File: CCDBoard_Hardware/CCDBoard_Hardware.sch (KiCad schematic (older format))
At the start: 19 parts

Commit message: Further Edits
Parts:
- removed C? (x3): C_Small, symbol Device:C_Small
- removed C? (x3): CP_Small, symbol Device:CP_Small
- added C? (x2): 0.1 µF, symbol Device:C_Small
- added C? (x2): 22 µF/25 V, symbol Device:CP_Small
- added Conn?: Molex_SL_04 IN, symbol MRDT_Connectors:Molex_SL_04
- added Conn?: Molex_SL_04 OUT, symbol MRDT_Connectors:Molex_SL_04
- added TP?: VideoTestPoint, symbol Connector:TestPoint
- added TP?: TrigTestPoint, symbol Connector:TestPoint
- added TP?: EOSTestPoint, symbol Connector:TestPoint
- added U?: LT1818, symbol pspice:OPAMP
- C? (x2): value C_Small -> 0.1 µF
- C? (x2): value CP_Small -> 22 µF/25 V
- C?: value C_Small -> 1 µF
- C?: value C_Small -> 22 pF
- R? (x2): value R -> 82 Ω
- R?: value R -> 100 Ω
- R?: value R -> 51 Ω
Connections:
- net +5V: now also C?.1, C?.1, C?.1, C?.1, Conn?.1, U?.4 (V+); no longer U?.~ (V-)
- net -IN: no longer R?.1
- net CLK: now also Conn?.3; no longer R?.2
- net EOS: now also Conn?.2, TP?.1; no longer U?.~ (Vss)
- net GND: now also C?.2, C?.2, C?.2, C?.2, Conn?.4, Conn?.4, U?.5 (V-)
- net ST: now also Conn?.2; no longer R?.1
- net Trig: now also Conn?.1, TP?.1; no longer U?.~ (Vss)
- net Video: now also Conn?.3, TP?.1; no longer R?.1
- net Trig_OUT: now reaches U?.~ (Vss)
- net Trig_OUT: now also U?.~ (Vcc)
- new net: R?.1, U?.1 (+)
- new net: R?.1, U?.2 (-), U?.3
- new net CLK_IN: R?.2, U?.~ (Vcc)
- new net EOS_OUT: U?.~ (Vcc), U?.~ (Vss)
- new net ST_IN: R?.1, U?.~ (Vcc)
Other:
- moved on the sheet: C?, R?, U?

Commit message: Added test points
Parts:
- removed U?: LT1818, symbol MRDT_ICs:LT1818
- added TP4: VideoPreAmpTestPoint, symbol Connector:TestPoint
- added TP5: CLKTestPoint, symbol Connector:TestPoint
- added TP6: STTestPoint, symbol Connector:TestPoint
- gave numbers to parts that had none: 22
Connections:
- net CLK: now also TP5.1
- net ST: now also TP6.1
- net at R3.2, U1.~ (Vss): now also TP4.1
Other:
- moved on the sheet: C6, C7, C8, R3, R4, TP1, U2

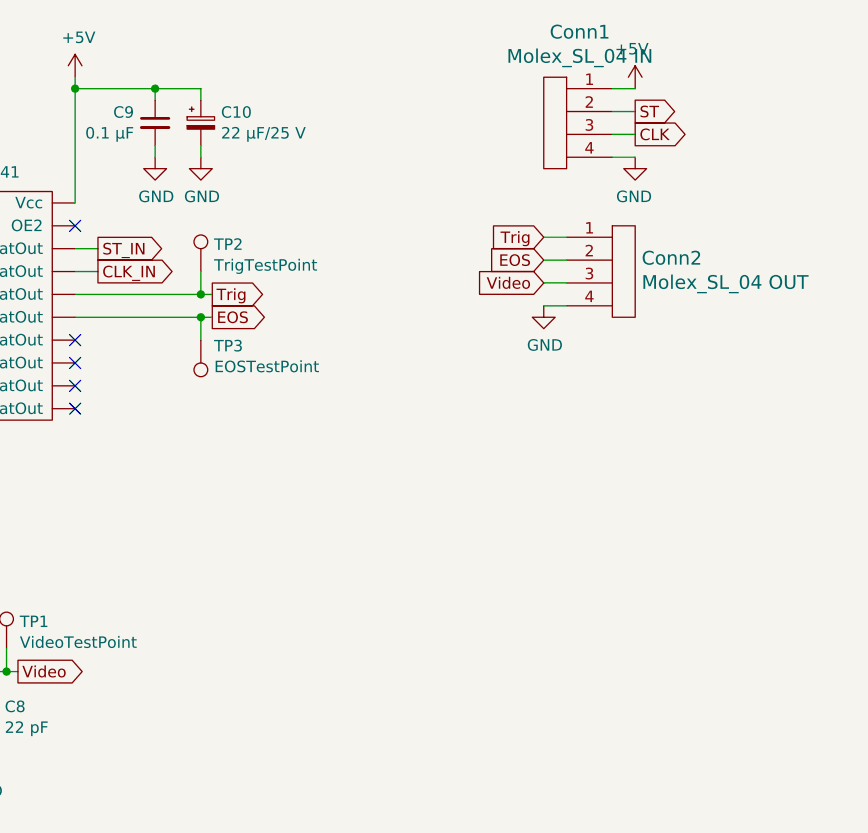
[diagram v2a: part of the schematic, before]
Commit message: Created and assigned footprints
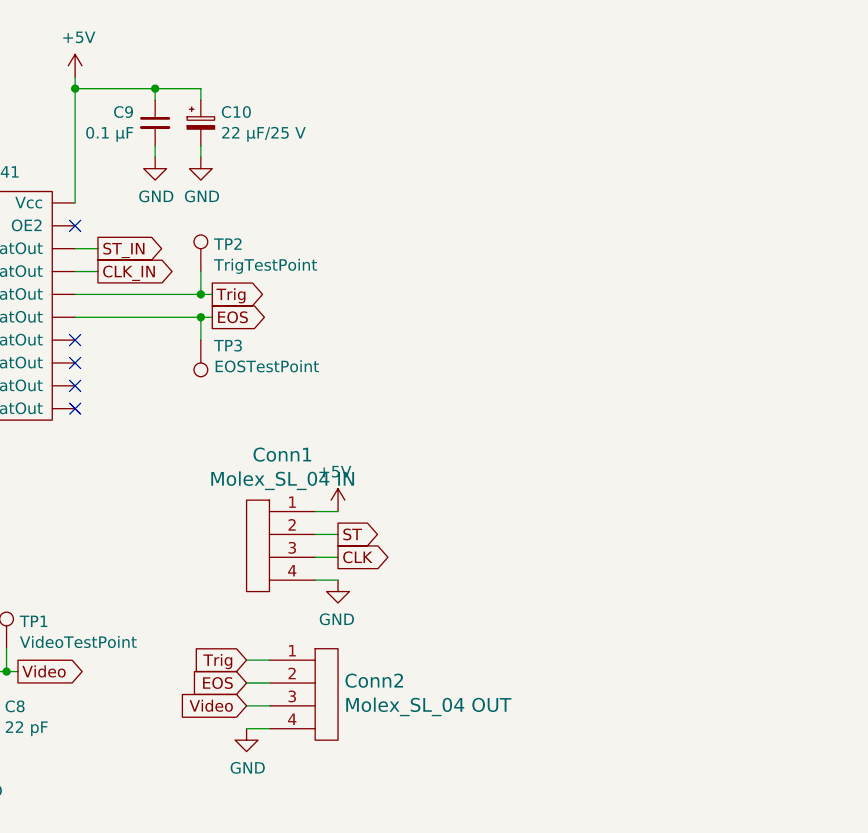
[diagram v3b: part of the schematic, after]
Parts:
- C1, C10, C4, C7: footprint (none) -> Capacitor_SMD:C_0805_2012Metric_Pad1.15x1.40mm_HandSolder
- C2, C3, C5, C6, C8, C9: footprint (none) -> Capacitor_SMD:C_0603_1608Metric_Pad1.05x0.95mm_HandSolder
- Conn1, Conn2: footprint (none) -> MRDT_Connectors:MOLEX_SL_04_Vertical
- R1, R2, R3, R4: footprint (none) -> Resistor_SMD:R_0603_1608Metric_Pad1.05x0.95mm_HandSolder
- TP1, TP2, TP3, TP4, TP5, TP6: footprint (none) -> TestPoint:TestPoint_THTPad_D2.5mm_Drill1.2mm
- U1: footprint (none) -> MRDT_Devices:CCD-S11639-01
- U2: footprint (none) -> Package_TO_SOT_SMD:SOT-23-5_HandSoldering
- U3: footprint (none) -> Package_SO:SOIC-20W_7.5x12.8mm_P1.27mm
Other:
- moved on the sheet: Conn1, Conn2
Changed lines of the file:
@@
 F 0 "U1" H 2950 2525 50  0000 C CNN
 F 1 "S11639-01" H 2950 2434 50  0000 C CNN
-F 2 "" H 2950 2400 50  0001 C CNN
+F 2 "MRDT_Devices:CCD-S11639-01" H 2950 2400 50  0001 C CNN
 F 3 "" H 2950 2400 50  0001 C CNN
 	1    2950 2400
@@
 F 0 "C3" H 2892 1946 50  0000 L CNN
 F 1 "0.1 µF" H 2892 1855 50  0000 L CNN
-F 2 "" H 2800 1900 50  0001 C CNN
+F 2 "Capacitor_SMD:C_0603_1608Metric_Pad1.05x0.95mm_HandSolder" H 2800 1900 50  0001 C CNN
 F 3 "~" H 2800 1900 50  0001 C CNN
 	1    2800 1900
@@
 F 0 "C4" H 3088 1946 50  0000 L CNN
 F 1 "22 µF/25 V" H 3088 1855 50  0000 L CNN
-F 2 "" H 3000 1900 50  0001 C CNN
+F 2 "Capacitor_SMD:C_0805_2012Metric_Pad1.15x1.40mm_HandSolder" H 3000 1900 50  0001 C CNN
 F 3 "~" H 3000 1900 50  0001 C CNN
 	1    3000 1900
@@
 F 0 "R1" V 2515 2700 50  0000 C CNN
 F 1 "82 Ω" V 2606 2700 50  0000 C CNN
-F 2 "" V 2330 2700 50  0001 C CNN
+F 2 "Resistor_SMD:R_0603_1608Metric_Pad1.05x0.95mm_HandSolder" V 2330 2700 50  0001 C CNN
 F 3 "~" H 2400 2700 50  0001 C CNN
 	1    2400 2700
@@
 F 0 "R2" V 3343 2500 50  0000 C CNN
 F 1 "82 Ω" V 3434 2500 50  0000 C CNN
-F 2 "" V 3480 2500 50  0001 C CNN
+F 2 "Resistor_SMD:R_0603_1608Metric_Pad1.05x0.95mm_HandSolder" V 3480 2500 50  0001 C CNN
 F 3 "~" H 3550 2500 50  0001 C CNN
 	1    3550 2500
@@
 F 0 "C5" H 3542 2896 50  0000 L CNN
 F 1 "1 µF" H 3542 2805 50  0000 L CNN
-F 2 "" H 3450 2850 50  0001 C CNN
+F 2 "Capacitor_SMD:C_0603_1608Metric_Pad1.05x0.95mm_HandSolder" H 3450 2850 50  0001 C CNN
 F 3 "~" H 3450 2850 50  0001 C CNN
 	1    3450 2850
@@
 F 0 "C1" H 2088 3896 50  0000 L CNN
 F 1 "22 µF/25 V" H 2088 3805 50  0000 L CNN
-F 2 "" H 2000 3850 50  0001 C CNN
+F 2 "Capacitor_SMD:C_0805_2012Metric_Pad1.15x1.40mm_HandSolder" H 2000 3850 50  0001 C CNN
 F 3 "~" H 2000 3850 50  0001 C CNN
 	1    2000 3850
@@
 F 0 "C2" H 2292 3896 50  0000 L CNN
 F 1 "0.1 µF" H 2292 3805 50  0000 L CNN
-F 2 "" H 2200 3850 50  0001 C CNN
+F 2 "Capacitor_SMD:C_0603_1608Metric_Pad1.05x0.95mm_HandSolder" H 2200 3850 50  0001 C CNN
 F 3 "~" H 2200 3850 50  0001 C CNN
 	1    2200 3850
@@
 F 0 "U3" H 5400 1675 50  0000 C CNN
 F 1 "74HC541" H 5400 1584 50  0000 C CNN
-F 2 "" H 5400 1550 50  0001 C CNN
+F 2 "Package_SO:SOIC-20W_7.5x12.8mm_P1.27mm" H 5400 1550 50  0001 C CNN
 F 3 "" H 5400 1550 50  0001 C CNN
 	1    5400 1550
@@
 F 0 "R3" V 3593 3600 50  0000 C CNN
 F 1 "100 Ω" V 3684 3600 50  0000 C CNN
-F 2 "" V 3730 3600 50  0001 C CNN
+F 2 "Resistor_SMD:R_0603_1608Metric_Pad1.05x0.95mm_HandSolder" V 3730 3600 50  0001 C CNN
 F 3 "~" H 3800 3600 50  0001 C CNN
 	1    3800 3600
@@
 F 0 "C9" H 6242 1346 50  0000 L CNN
 F 1 "0.1 µF" H 6242 1255 50  0000 L CNN
-F 2 "" H 6150 1300 50  0001 C CNN
+F 2 "Capacitor_SMD:C_0603_1608Metric_Pad1.05x0.95mm_HandSolder" H 6150 1300 50  0001 C CNN
 F 3 "~" H 6150 1300 50  0001 C CNN
 	1    6150 1300
@@
 F 0 "C10" H 6438 1346 50  0000 L CNN
 F 1 "22 µF/25 V" H 6438 1255 50  0000 L CNN
-F 2 "" H 6350 1300 50  0001 C CNN
+F 2 "Capacitor_SMD:C_0805_2012Metric_Pad1.15x1.40mm_HandSolder" H 6350 1300 50  0001 C CNN
 F 3 "~" H 6350 1300 50  0001 C CNN
 	1    6350 1300
@@
 F 0 "TP1" H 5558 3718 50  0000 L CNN
 F 1 "VideoTestPoint" H 5558 3627 50  0000 L CNN
-F 2 "" H 5700 3600 50  0001 C CNN
+F 2 "TestPoint:TestPoint_THTPad_D2.5mm_Drill1.2mm" H 5700 3600 50  0001 C CNN
 F 3 "~" H 5700 3600 50  0001 C CNN
 	1    5500 3600
@@
 F 0 "U2" H 4694 3746 50  0000 L CNN
 F 1 "LT1818" H 4694 3655 50  0000 L CNN
-F 2 "" H 4350 3700 50  0001 C CNN
+F 2 "Package_TO_SOT_SMD:SOT-23-5_HandSoldering" H 4350 3700 50  0001 C CNN
 F 3 "~" H 4350 3700 50  0001 C CNN
 	1    4350 3700
@@
 F 0 "R4" V 4943 3700 50  0000 C CNN
 F 1 "51 Ω" V 5034 3700 50  0000 C CNN
-F 2 "" V 5080 3700 50  0001 C CNN
+F 2 "Resistor_SMD:R_0603_1608Metric_Pad1.05x0.95mm_HandSolder" V 5080 3700 50  0001 C CNN
 F 3 "~" H 5150 3700 50  0001 C CNN
 	1    5150 3700
@@
 F 0 "C8" H 5492 3946 50  0000 L CNN
 F 1 "22 pF" H 5492 3855 50  0000 L CNN
-F 2 "" H 5400 3900 50  0001 C CNN
+F 2 "Capacitor_SMD:C_0603_1608Metric_Pad1.05x0.95mm_HandSolder" H 5400 3900 50  0001 C CNN
 F 3 "~" H 5400 3900 50  0001 C CNN
 	1    5400 3900
@@
 F 0 "C6" H 4692 3096 50  0000 L CNN
 F 1 "0.1 µF" H 4692 3005 50  0000 L CNN
-F 2 "" H 4600 3050 50  0001 C CNN
+F 2 "Capacitor_SMD:C_0603_1608Metric_Pad1.05x0.95mm_HandSolder" H 4600 3050 50  0001 C CNN
 F 3 "~" H 4600 3050 50  0001 C CNN
 	1    4600 3050
@@
 F 0 "C7" H 4888 3096 50  0000 L CNN
 F 1 "22 µF/25 V" H 4888 3005 50  0000 L CNN
-F 2 "" H 4800 3050 50  0001 C CNN
+F 2 "Capacitor_SMD:C_0805_2012Metric_Pad1.15x1.40mm_HandSolder" H 4800 3050 50  0001 C CNN
 F 3 "~" H 4800 3050 50  0001 C CNN
 	1    4800 3050
@@
 F 0 "TP2" H 6408 2068 50  0000 L CNN
 F 1 "TrigTestPoint" H 6408 1977 50  0000 L CNN
-F 2 "" H 6550 1950 50  0001 C CNN
+F 2 "TestPoint:TestPoint_THTPad_D2.5mm_Drill1.2mm" H 6550 1950 50  0001 C CNN
 F 3 "~" H 6550 1950 50  0001 C CNN
 	1    6350 1950
@@
 F 0 "TP3" H 6292 2276 50  0000 R CNN
 F 1 "EOSTestPoint" H 6292 2367 50  0000 R CNN
-F 2 "" H 6550 2250 50  0001 C CNN
+F 2 "TestPoint:TestPoint_THTPad_D2.5mm_Drill1.2mm" H 6550 2250 50  0001 C CNN
 F 3 "~" H 6550 2250 50  0001 C CNN
 	1    6350 2250
@@
 L MRDT_Connectors:Molex_SL_04 Conn1
 U 1 1 5DA4FD22
-P 7950 1500
-F 0 "Conn1" H 7892 2097 60  0000 C CNN
-F 1 "Molex_SL_04 IN" H 7892 1991 60  0000 C CNN
-F 2 "" H 7950 1500 60  0001 C CNN
-F 3 "" H 7950 1500 60  0001 C CNN
-	1    7950 1500
+P 6650 3350
+F 0 "Conn1" H 6592 3947 60  0000 C CNN
+F 1 "Molex_SL_04 IN" H 6592 3841 60  0000 C CNN
+F 2 "MRDT_Connectors:MOLEX_SL_04_Vertical" H 6650 3350 60  0001 C CNN
+F 3 "" H 6650 3350 60  0001 C CNN
+	1    6650 3350
 	-1   0    0    -1
 $EndComp
@@
 L MRDT_Connectors:Molex_SL_04 Conn2
 U 1 1 5DA5117C
-P 8150 2150
-F 0 "Conn2" H 8278 2408 60  0000 L CNN
-F 1 "Molex_SL_04 OUT" H 8278 2302 60  0000 L CNN
-F 2 "" H 8150 2150 60  0001 C CNN
-F 3 "" H 8150 2150 60  0001 C CNN
-	1    8150 2150
+P 6850 4000
+F 0 "Conn2" H 6978 4258 60  0000 L CNN
+F 1 "Molex_SL_04 OUT" H 6978 4152 60  0000 L CNN
+F 2 "MRDT_Connectors:MOLEX_SL_04_Vertical" H 6850 4000 60  0001 C CNN
+F 3 "" H 6850 4000 60  0001 C CNN
+	1    6850 4000
 	1    0    0    -1
 $EndComp
@@
 L power:+5V #PWR0119
 U 1 1 5DA51C7E
-P 8250 1150
-F 0 "#PWR0119" H 8250 1000 50  0001 C CNN
-F 1 "+5V" H 8265 1323 50  0000 C CNN
-F 2 "" H 8250 1150 50  0001 C CNN
-F 3 "" H 8250 1150 50  0001 C CNN
-	1    8250 1150
+P 6950 3000
+F 0 "#PWR0119" H 6950 2850 50  0001 C CNN
+F 1 "+5V" H 6965 3173 50  0000 C CNN
+F 2 "" H 6950 3000 50  0001 C CNN
+F 3 "" H 6950 3000 50  0001 C CNN
+	1    6950 3000
 	-1   0    0    -1
 $EndComp
 Wire Wire Line
-	8150 1150 8250 1150
-Wire Wire Line
-	8150 1250 8250 1250
-Wire Wire Line
-	8150 1350 8250 1350
-Wire Wire Line
-	8150 1450 8250 1450
-Text GLabel 8250 1250 2    50   Output ~ 0
+	6850 3000 6950 3000
+Wire Wire Line
+	6850 3100 6950 3100
+Wire Wire Line
+	6850 3200 6950 3200
+Wire Wire Line
+	6850 3300 6950 3300
+Text GLabel 6950 3100 2    50   Output ~ 0
 ST
-Text GLabel 8250 1350 2    50   Output ~ 0
+Text GLabel 6950 3200 2    50   Output ~ 0
 CLK
 $Comp
 L power:GND #PWR0120
 U 1 1 5DA592EF
-P 8250 1450
-F 0 "#PWR0120" H 8250 1200 50  0001 C CNN
-F 1 "GND" H 8255 1277 50  0000 C CNN
-F 2 "" H 8250 1450 50  0001 C CNN
-F 3 "" H 8250 1450 50  0001 C CNN
-	1    8250 1450
+P 6950 3300
+F 0 "#PWR0120" H 6950 3050 50  0001 C CNN
+F 1 "GND" H 6955 3127 50  0000 C CNN
+F 2 "" H 6950 3300 50  0001 C CNN
+F 3 "" H 6950 3300 50  0001 C CNN
+	1    6950 3300
 	-1   0    0    -1
 $EndComp
 Wire Wire Line
-	7950 1800 7850 1800
-Wire Wire Line
-	7850 1900 7950 1900
-Wire Wire Line
-	7950 2000 7850 2000
-Wire Wire Line
-	7850 2100 7950 2100
-Text GLabel 7850 1800 0    50   Input ~ 0
+	6650 3650 6550 3650
+Wire Wire Line
+	6550 3750 6650 3750
+Wire Wire Line
+	6650 3850 6550 3850
+Wire Wire Line
+	6550 3950 6650 3950
+Text GLabel 6550 3650 0    50   Input ~ 0
 Trig
-Text GLabel 7850 1900 0    50   Input ~ 0
+Text GLabel 6550 3750 0    50   Input ~ 0
 EOS
-Text GLabel 7850 2000 0    50   Input ~ 0
+Text GLabel 6550 3850 0    50   Input ~ 0
 Video
 $Comp
 L power:GND #PWR0121
 U 1 1 5DA67070
-P 7850 2100
-F 0 "#PWR0121" H 7850 1850 50  0001 C CNN
-F 1 "GND" H 7855 1927 50  0000 C CNN
-F 2 "" H 7850 2100 50  0001 C CNN
-F 3 "" H 7850 2100 50  0001 C CNN
-	1    7850 2100
+P 6550 3950
+F 0 "#PWR0121" H 6550 3700 50  0001 C CNN
+F 1 "GND" H 6555 3777 50  0000 C CNN
+F 2 "" H 6550 3950 50  0001 C CNN
+F 3 "" H 6550 3950 50  0001 C CNN
+	1    6550 3950
 	1    0    0    -1
 $EndComp
@@
 F 0 "TP5" H 4758 1768 50  0000 L CNN
 F 1 "CLKTestPoint" H 4758 1677 50  0000 L CNN
-F 2 "" H 4900 1650 50  0001 C CNN
+F 2 "TestPoint:TestPoint_THTPad_D2.5mm_Drill1.2mm" H 4900 1650 50  0001 C CNN
 F 3 "~" H 4900 1650 50  0001 C CNN
 	1    4700 1650
@@
 F 0 "TP6" H 4958 1768 50  0000 L CNN
 F 1 "STTestPoint" H 4958 1677 50  0000 L CNN
-F 2 "" H 5100 1650 50  0001 C CNN
+F 2 "TestPoint:TestPoint_THTPad_D2.5mm_Drill1.2mm" H 5100 1650 50  0001 C CNN
 F 3 "~" H 5100 1650 50  0001 C CNN
 	1    4900 1650
@@
 F 0 "TP4" H 3342 3726 50  0000 R CNN
 F 1 "VideoPreAmpTestPoint" H 3342 3817 50  0000 R CNN
-F 2 "" H 3600 3700 50  0001 C CNN
+F 2 "TestPoint:TestPoint_THTPad_D2.5mm_Drill1.2mm" H 3600 3700 50  0001 C CNN
 F 3 "~" H 3600 3700 50  0001 C CNN
 	1    3400 3700
